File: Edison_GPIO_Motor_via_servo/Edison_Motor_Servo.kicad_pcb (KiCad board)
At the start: 2 copper layers, 27.9 x 27.9 mm, 6 parts, among them P5 CONN_01X10, P6 CONN_01X10

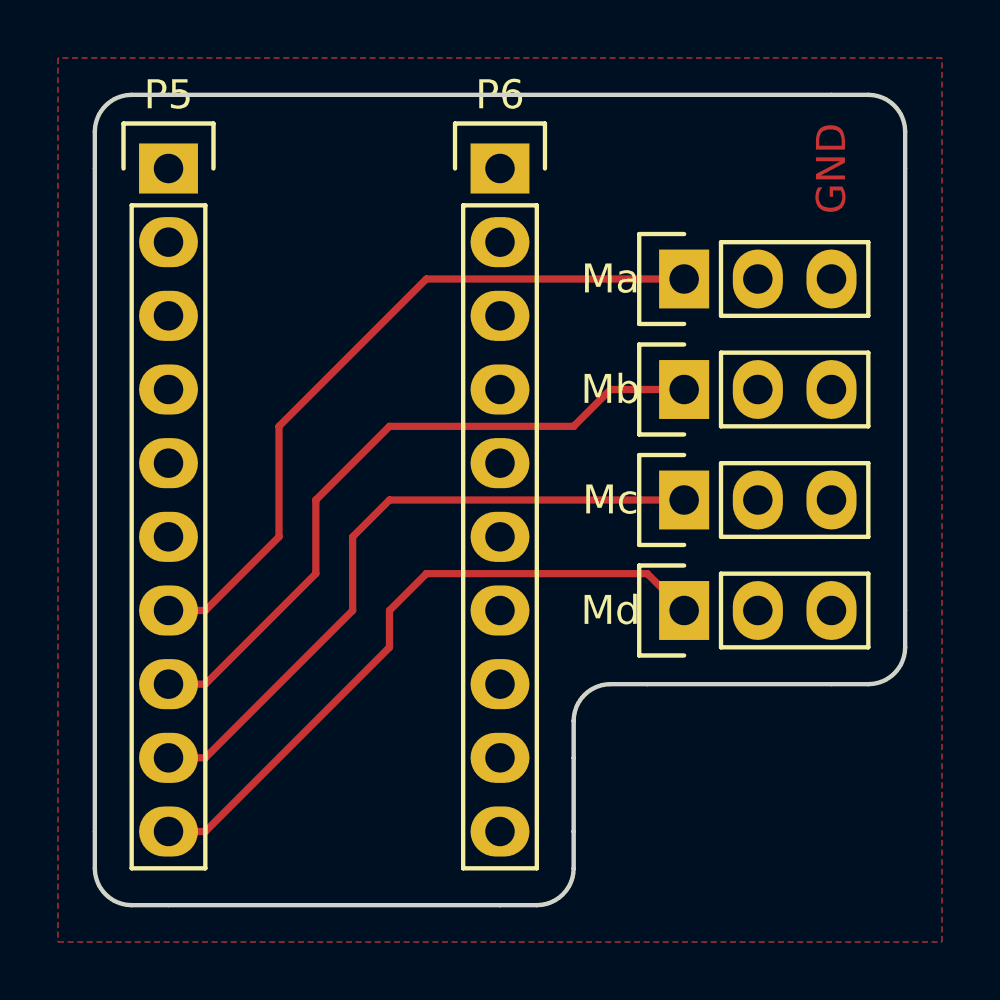
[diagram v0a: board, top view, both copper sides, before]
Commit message: updated open-loop system model, added screenshot of motor response graph
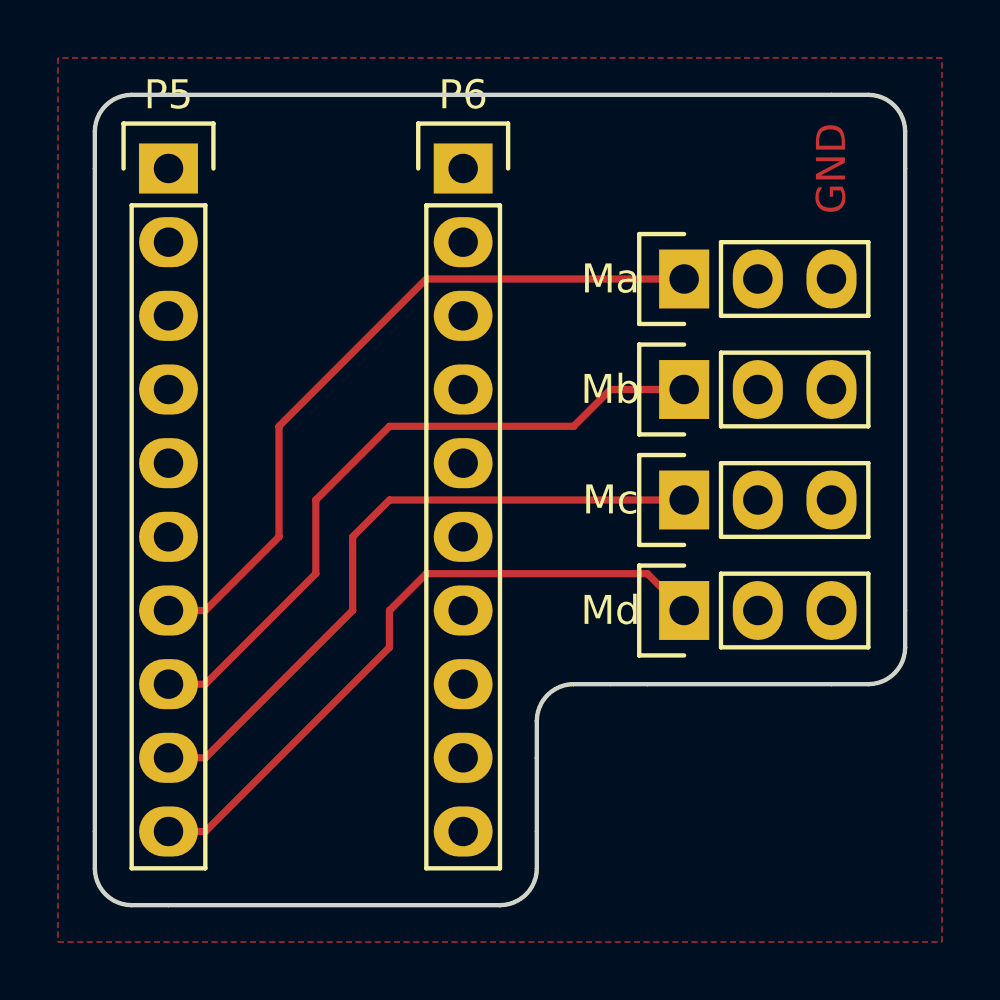
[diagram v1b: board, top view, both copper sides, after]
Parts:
- moved P6 1.27 mm to (133.3, 91.4)
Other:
- outline, holes or cut-outs redrawn
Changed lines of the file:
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@@
     (visible_elements FFFFFF7F)
     (pcbplotparams
-      (layerselection 0x00080_00000001)
+      (layerselection 0x01080_00000001)
       (usegerberextensions false)
       (excludeedgelayer true)
@@
   )
   (module Socket_Strips:Socket_Strip_Straight_1x10 (layer F.Cu)
-    (at 134.62 91.44 270)
+    (at 133.35 91.44 270)
     (descr "Through hole socket strip")
     (tags "socket strip")
@@
     )
   )
+  (gr_line (start 137.16 109.22) (end 138.43 109.22) (angle 90) (layer Edge.Cuts) (width 0.15))
   (gr_text GND (at 146.05 91.44 90) (layer F.Cu)
     (effects (font (size 1 1) (thickness 0.25)))
@@
   (gr_line (start 120.65 115.57) (end 120.65 114.3) (angle 90) (layer Edge.Cuts) (width 0.15))
   (gr_line (start 123.19 116.84) (end 121.92 116.84) (angle 90) (layer Edge.Cuts) (width 0.15))
-  (gr_line (start 135.89 116.84) (end 134.62 116.84) (angle 90) (layer Edge.Cuts) (width 0.15))
-  (gr_line (start 137.16 114.3) (end 137.16 115.57) (angle 90) (layer Edge.Cuts) (width 0.15))
-  (gr_line (start 137.16 110.49) (end 137.16 111.76) (angle 90) (layer Edge.Cuts) (width 0.15))
+  (gr_line (start 135.89 114.3) (end 135.89 115.57) (angle 90) (layer Edge.Cuts) (width 0.15))
+  (gr_line (start 135.89 110.49) (end 135.89 111.76) (angle 90) (layer Edge.Cuts) (width 0.15))
   (gr_line (start 139.7 109.22) (end 138.43 109.22) (angle 90) (layer Edge.Cuts) (width 0.15))
   (gr_line (start 147.32 109.22) (end 146.05 109.22) (angle 90) (layer Edge.Cuts) (width 0.15))
@@
   (gr_line (start 147.32 88.9) (end 146.05 88.9) (angle 90) (layer Edge.Cuts) (width 0.15))
   (gr_arc (start 147.32 107.95) (end 148.59 107.95) (angle 90) (layer Edge.Cuts) (width 0.15))
-  (gr_arc (start 138.43 110.49) (end 137.16 110.49) (angle 90) (layer Edge.Cuts) (width 0.15))
-  (gr_arc (start 135.89 115.57) (end 137.16 115.57) (angle 90) (layer Edge.Cuts) (width 0.15))
+  (gr_arc (start 137.16 110.49) (end 135.89 110.49) (angle 90) (layer Edge.Cuts) (width 0.15))
+  (gr_arc (start 134.62 115.57) (end 135.89 115.57) (angle 90) (layer Edge.Cuts) (width 0.15))
   (gr_arc (start 121.92 115.57) (end 121.92 116.84) (angle 90) (layer Edge.Cuts) (width 0.15))
   (gr_arc (start 121.92 90.17) (end 120.65 90.17) (angle 90) (layer Edge.Cuts) (width 0.15))
@@
   (gr_line (start 120.65 114.3) (end 120.65 91.44) (angle 90) (layer Edge.Cuts) (width 0.15))
   (gr_line (start 134.62 116.84) (end 123.19 116.84) (angle 90) (layer Edge.Cuts) (width 0.15))
-  (gr_line (start 137.16 111.76) (end 137.16 114.3) (angle 90) (layer Edge.Cuts) (width 0.15))
+  (gr_line (start 135.89 111.76) (end 135.89 114.3) (angle 90) (layer Edge.Cuts) (width 0.15))
   (gr_line (start 146.05 109.22) (end 139.7 109.22) (angle 90) (layer Edge.Cuts) (width 0.15))
   (gr_line (start 148.59 91.44) (end 148.59 106.68) (angle 90) (layer Edge.Cuts) (width 0.15))
@@
   (gr_line (start 120.65 88.9) (end 148.59 88.9) (angle 90) (layer Eco1.User) (width 0.2))
   (gr_line (start 120.65 116.84) (end 120.65 88.9) (angle 90) (layer Eco1.User) (width 0.2))
-  (segment (start 123.19 106.68) (end 124.46 106.68) (width 0.25) (layer F.Cu) (net 1) (status 400000))
-  (segment (start 132.08 95.25) (end 140.97 95.25) (width 0.25) (layer F.Cu) (net 1) (status 800000))
+  (segment (start 123.19 106.68) (end 124.46 106.68) (width 0.25) (layer F.Cu) (net 1))
+  (segment (start 132.08 95.25) (end 140.97 95.25) (width 0.25) (layer F.Cu) (net 1))
   (segment (start 127 100.33) (end 132.08 95.25) (width 0.25) (layer F.Cu) (net 1))
   (segment (start 127 104.14) (end 127 100.33) (width 0.25) (layer F.Cu) (net 1))
@@
   (segment (start 128.27 105.41) (end 128.27 102.87) (width 0.25) (layer F.Cu) (net 22))
   (segment (start 128.27 102.87) (end 130.81 100.33) (width 0.25) (layer F.Cu) (net 22))
-  (segment (start 123.19 109.22) (end 124.46 109.22) (width 0.25) (layer F.Cu) (net 22) (status 400000))
-  (segment (start 138.43 99.06) (end 140.97 99.06) (width 0.25) (layer F.Cu) (net 22) (status 800000))
+  (segment (start 123.19 109.22) (end 124.46 109.22) (width 0.25) (layer F.Cu) (net 22))
+  (segment (start 138.43 99.06) (end 140.97 99.06) (width 0.25) (layer F.Cu) (net 22))
   (segment (start 137.16 100.33) (end 138.43 99.06) (width 0.25) (layer F.Cu) (net 22))
-  (segment (start 123.19 111.76) (end 124.46 111.76) (width 0.25) (layer F.Cu) (net 23) (status 400000))
-  (segment (start 130.81 102.87) (end 140.97 102.87) (width 0.25) (layer F.Cu) (net 23) (status 800000))
+  (segment (start 123.19 111.76) (end 124.46 111.76) (width 0.25) (layer F.Cu) (net 23))
+  (segment (start 130.81 102.87) (end 140.97 102.87) (width 0.25) (layer F.Cu) (net 23))
   (segment (start 129.54 104.14) (end 130.81 102.87) (width 0.25) (layer F.Cu) (net 23))
   (segment (start 129.54 106.68) (end 129.54 104.14) (width 0.25) (layer F.Cu) (net 23))
   (segment (start 124.46 111.76) (end 129.54 106.68) (width 0.25) (layer F.Cu) (net 23))
-  (segment (start 123.19 114.3) (end 124.46 114.3) (width 0.25) (layer F.Cu) (net 24) (status 400000))
-  (segment (start 139.7 105.41) (end 140.97 106.68) (width 0.25) (layer F.Cu) (net 24) (status 800000))
+  (segment (start 123.19 114.3) (end 124.46 114.3) (width 0.25) (layer F.Cu) (net 24))
+  (segment (start 139.7 105.41) (end 140.97 106.68) (width 0.25) (layer F.Cu) (net 24))
   (segment (start 132.08 105.41) (end 139.7 105.41) (width 0.25) (layer F.Cu) (net 24))
   (segment (start 130.81 106.68) (end 132.08 105.41) (width 0.25) (layer F.Cu) (net 24))
